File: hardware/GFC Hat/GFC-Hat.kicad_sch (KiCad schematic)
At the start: 31 parts, among them U3 CAT24C32WI-GT3, U4 SAM-M8Q, U6 BME280

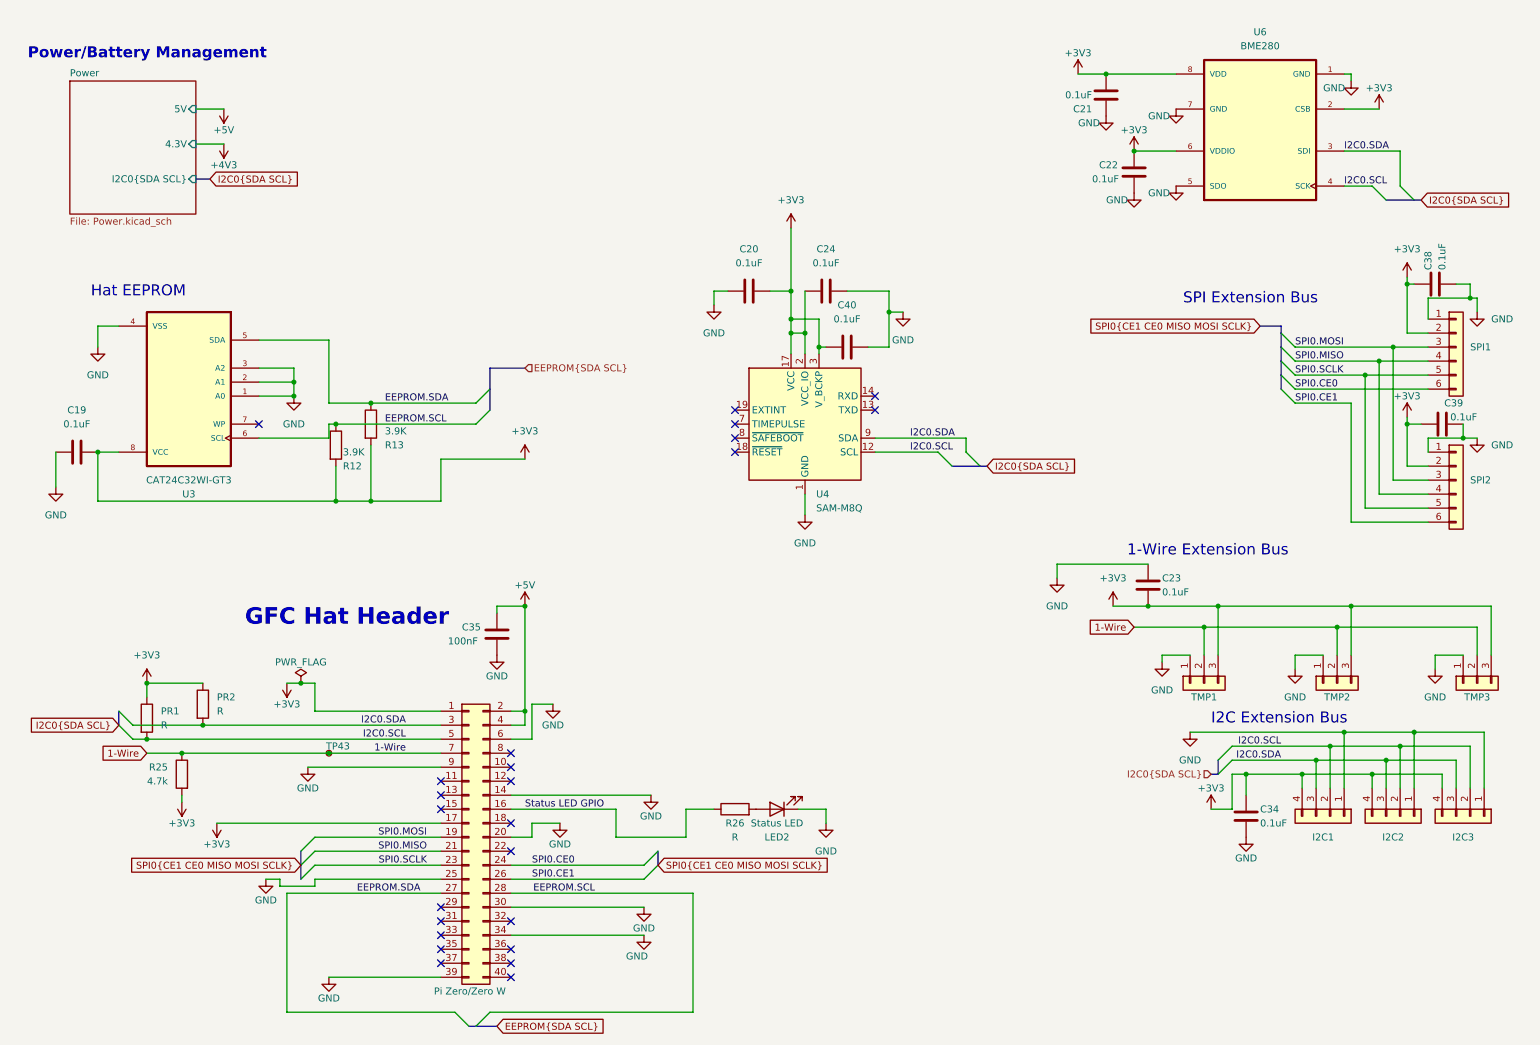
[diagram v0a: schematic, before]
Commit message: Hardware refresh, removed layered sheets and split hat and shoe
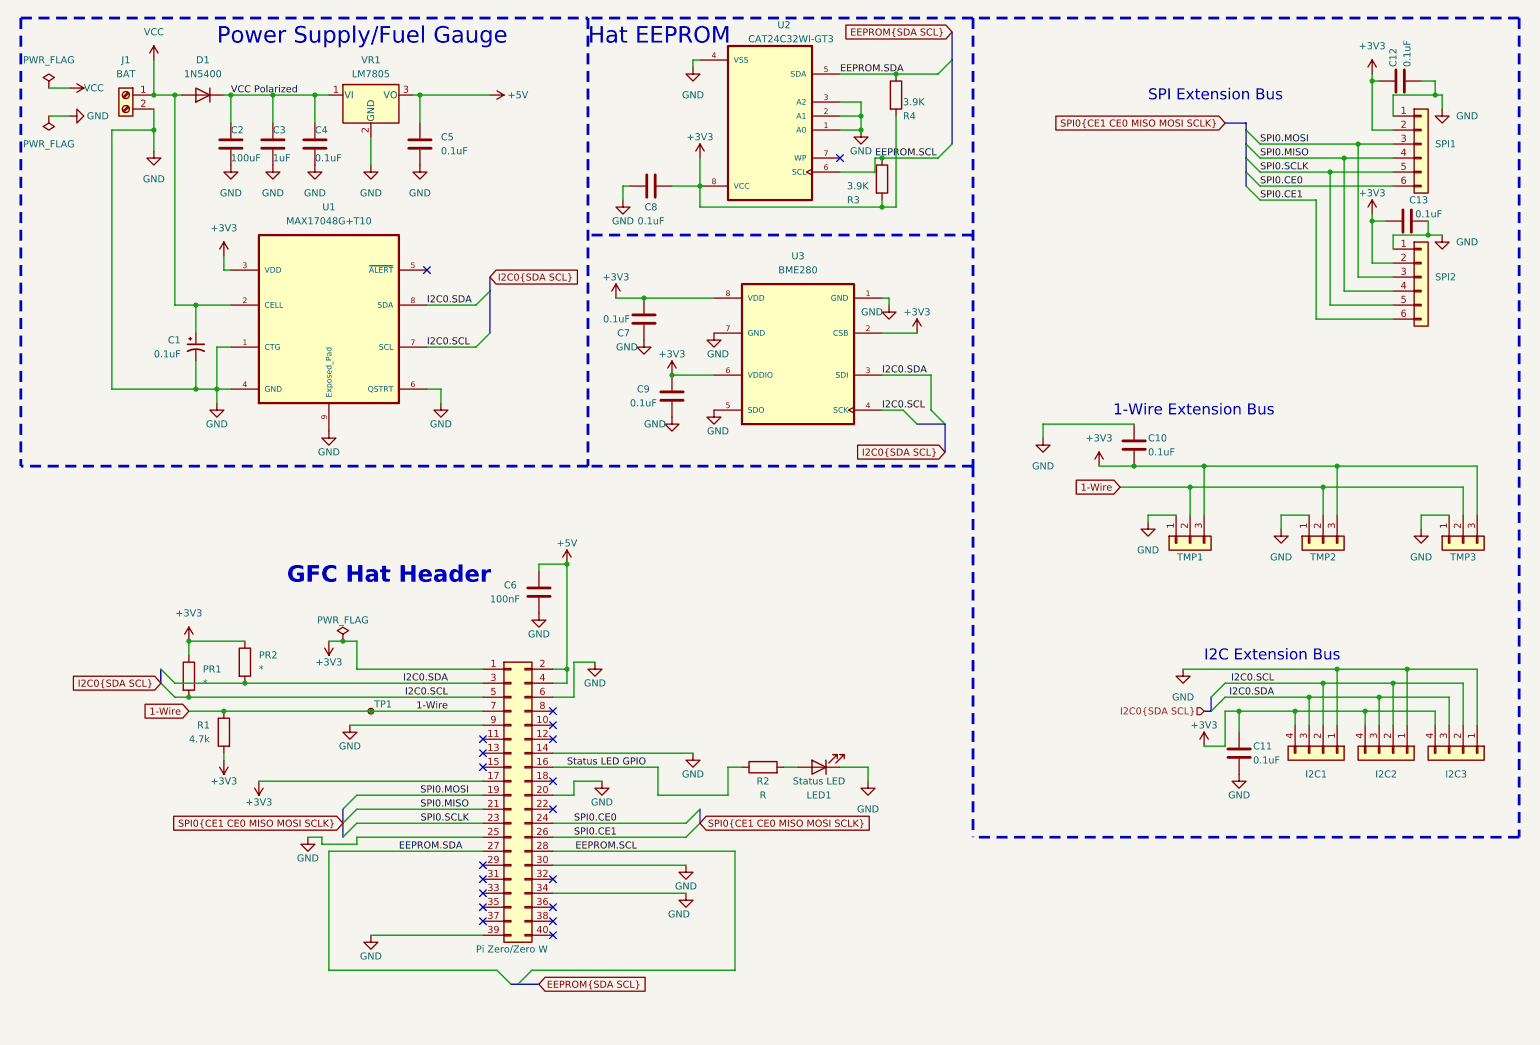
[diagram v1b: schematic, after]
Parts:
- removed C20, C24, C40: 0.1uF, Capacitor_SMD:C_0603_1608Metric_Pad1.08x0.95mm_HandSolder, symbol Device:C
- removed U4: SAM-M8Q, RF_GPS:ublox_SAM-M8Q, symbol RF_GPS:SAM-M8Q
- added C1: 0.1uF, Capacitor_SMD:C_0603_1608Metric_Pad1.08x0.95mm_HandSolder, symbol Device:C_Polarized_Small_US
- added C2: 100uF, Capacitor_THT:CP_Radial_D6.3mm_P2.50mm, symbol Device:C
- added C3: 1uF, Capacitor_SMD:C_0603_1608Metric_Pad1.08x0.95mm_HandSolder, symbol Device:C
- added C4, C5: 0.1uF, Capacitor_SMD:C_0603_1608Metric_Pad1.08x0.95mm_HandSolder, symbol Device:C
- added D1: 1N5400, Diode_THT:D_DO-15_P12.70mm_Horizontal, symbol Diode:1N5400
- added J1: BAT, Connector_PinHeader_2.54mm:PinHeader_1x02_P2.54mm_Vertical, symbol Connector:Screw_Terminal_01x02
- added U1: MAX17048G+T10, MAX17048G_T10:SON50P200X200X80-9N, symbol MAX17048G_T10:MAX17048G+T10
- added VR1: LM7805, Package_TO_SOT_SMD:TO-263-3_TabPin2, symbol Regulator_Linear:LM7805_TO220
- PR1, PR2: value R -> *
- renumbered C23 to C10, C34 to C11, C38 to C12, C39 to C13, C35 to C6, C21 to C7, C19 to C8, C22 to C9, CPU2 to CPU1, LED2 to LED1, R25 to R1, R26 to R2, R12 to R3, R13 to R4, TP43 to TP1, U3 to U2, U6 to U3
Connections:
- net +3V3: now also U1.3 (VDD)
- net +5V: now also C5.1, VR1.3 (VO)
- net GND: now also C1.2, C2.2, C3.2, C4.2, C5.2, J1.2 (Pin_2), U1.1 (CTG), U1.4 (GND), U1.6 (QSTRT), U1.9 (Exposed_Pad), VR1.2 (GND)
- net I2C0.SCL: now also U1.7 (SCL)
- net I2C0.SDA: now also U1.8 (SDA)
- new net VCC: C1.1, D1.2 (A), J1.1 (Pin_1), U1.2 (CELL)
- new net VCC Polarized: C2.1, C3.1, C4.1, D1.1 (K), VR1.1 (VI)
- no-connect marks 24 -> 19
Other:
- removed sheet Power
- note added: "Power Supply/Fuel Gauge"
- note removed: "Power/Battery Management"
- moved on the sheet: C10, C11, C12, C13, C6, C7, C8, C9, I2C1, I2C2, I2C3, LED1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

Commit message: Started making some revisions to Prototype 2, cleaned up files.
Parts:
- removed I2C3: I2C0, Connector_PinHeader_2.00mm:PinHeader_1x04_P2.00mm_Vertical, symbol Connector_Generic:Conn_01x04
- removed LED1: Status LED, LED_SMD:LED_0805_2012Metric, symbol Device:LED
- removed R2: R, Resistor_SMD:R_0603_1608Metric_Pad0.98x0.95mm_HandSolder, symbol Device:R
- removed TMP3: 1-Wire Bus, Connector_PinHeader_2.00mm:PinHeader_1x03_P2.00mm_Vertical, symbol Connector_Generic:Conn_01x03
- removed TP1: Test Point, TestPoint:TestPoint_Pad_D1.0mm, symbol Connector:TestPoint_Small
- added C12, C13, C14, C17, C18: 0.1uF, Capacitor_SMD:C_0603_1608Metric_Pad1.08x0.95mm_HandSolder, symbol Device:C
- added U4: DS18B20, Package_TO_SOT_THT:TO-92_Inline, symbol Sensor_Temperature:DS18B20
- 1W1: renamed from TMP1; footprint Connector_PinHeader_2.00mm:PinHeader_1x03_P2.00mm_Vertical -> GFC-Hat-Footprints:JST_PH_B3B-PH-K_1x03_P2.00mm_Vertical; DESCRIPTION (none) -> JST B3B-PH-K-S; Digikey https://www.digikey.com/short/bd73wft8 -> https://www.digikey.com/en/products/detail/jst-sales-americ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
- 1W2: renamed from TMP2; footprint Connector_PinHeader_2.00mm:PinHeader_1x03_P2.00mm_Vertical -> GFC-Hat-Footprints:JST_PH_B3B-PH-K_1x03_P2.00mm_Vertical; DESCRIPTION (none) -> JST B3B-PH-K-S; Digikey https://www.digikey.com/short/bd73wft8 -> https://www.digikey.com/en/products/detail/jst-sales-americ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
- C1: renamed from C2; footprint Capacitor_THT:CP_Radial_D6.3mm_P2.50mm -> Capacitor_SMD:C_Elec_6.3x7.7; Digikey https://www.digikey.com/en/products/detail/cornell-dubilier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 -> (none)
- C10, C11, C7, C8, C9: Digikey https://www.digikey.com/short/3wn2fdb2 -> (none)
- C15: renamed from C12; Digikey https://www.digikey.com/short/3wn2fdb2 -> (none)
- C16: renamed from C13; Digikey https://www.digikey.com/short/3wn2fdb2 -> (none)
- C2: renamed from C3; footprint Capacitor_SMD:C_0603_1608Metric_Pad1.08x0.95mm_HandSolder -> Capacitor_SMD:C_0805_2012Metric_Pad1.18x1.45mm_HandSolder; DESCRIPTION (none) -> CL21B105KAFNNNE; Digikey https://www.digikey.com/short/mb0p55bt -> https://www.digikey.com/en/products/detail/samsung-electro-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
- C3: renamed from C4; Digikey https://www.digikey.com/short/3wn2fdb2 -> (none)
- C4: renamed from C5; Digikey https://www.digikey.com/short/3wn2fdb2 -> (none)
- C5: renamed from C1; Digikey https://www.digikey.com/short/3wn2fdb2 -> (none)
- C6: value 100nF -> 0.1uF; Unit Price (none) -> 0.10
- D1: value 1N5400 -> 2A LFV; footprint Diode_THT:D_DO-15_P12.70mm_Horizontal -> Diode_SMD:D_SMA_Handsoldering; symbol Diode:1N5400 -> GFC-Symbols:1N5400; Digikey https://www.digikey.com/short/p7bpz43m -> (none)
- I2C1, I2C2: footprint Connector_PinHeader_2.00mm:PinHeader_1x04_P2.00mm_Vertical -> GFC-Hat-Footprints:JST_PH_B4B-PH-K_1x04_P2.00mm_Vertical; DESCRIPTION (none) -> JST B4B-PH-K-S; Digikey (none) -> https://www.digikey.com/en/products/detail/jst-sales-americ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
- J1: footprint Connector_PinHeader_2.54mm:PinHeader_1x02_P2.54mm_Vertical -> GFC-Hat-Footprints:OSTVN02A150 2x1 Terminal Block
- PI_HDR1: renamed from CPU1; value Pi Zero/Zero W -> PI Header; Digikey N/A -> (none)
- SPI1, SPI2: footprint Connector_PinHeader_2.00mm:PinHeader_1x06_P2.00mm_Vertical -> GFC-Hat-Footprints:JST_PH_B6B-PH-K_1x06_P2.00mm_Vertical; DESCRIPTION (none) -> JST B6B-PH-K-S
- U1: symbol MAX17048G_T10:MAX17048G+T10 -> GFC-Symbols:MAX17048G+T10
- U2: renamed from U3; symbol BME280:BME280 -> GFC-Symbols:BME280
- U3: renamed from U2; symbol EEPROM:CAT24C32WI-GT3 -> GFC-Symbols:CAT24C32WI-GT3
- VR1: symbol Regulator_Linear:LM7805_TO220 -> GFC-Symbols:LM7805_TO220
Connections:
- net +3V3: now also C12.2, C13.2, C14.2, C17.1, C18.1, U4.3 (VDD); no longer C10.1, R3.2, R4.2
- net 1-Wire: now also U4.2 (DQ)
- net GND: now also C10.1, R3.2, R4.2, C12.1, C13.1, C14.1, C17.2, C18.2, U4.1 (GND)
- net Status LED GPIO: no longer names the net of PI_HDR1.16 (Pin_16)
- no-connect marks 19 -> 20
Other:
- note added: "Hat Header"
- note removed: "GFC Hat Header"
- title: (none) -> Giraffe Flight Computer (GFC) Hat
- moved on the sheet: 1W1, 1W2, C11, C8, I2C1, I2C2
